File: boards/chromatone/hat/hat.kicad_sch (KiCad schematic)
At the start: 55 parts, among them J1 Pi 40-pin, J2 Strip, J3 Line out, U1 ISO7720D, U2 PCM5102A, U3 ME6211C33, U4 24LC32

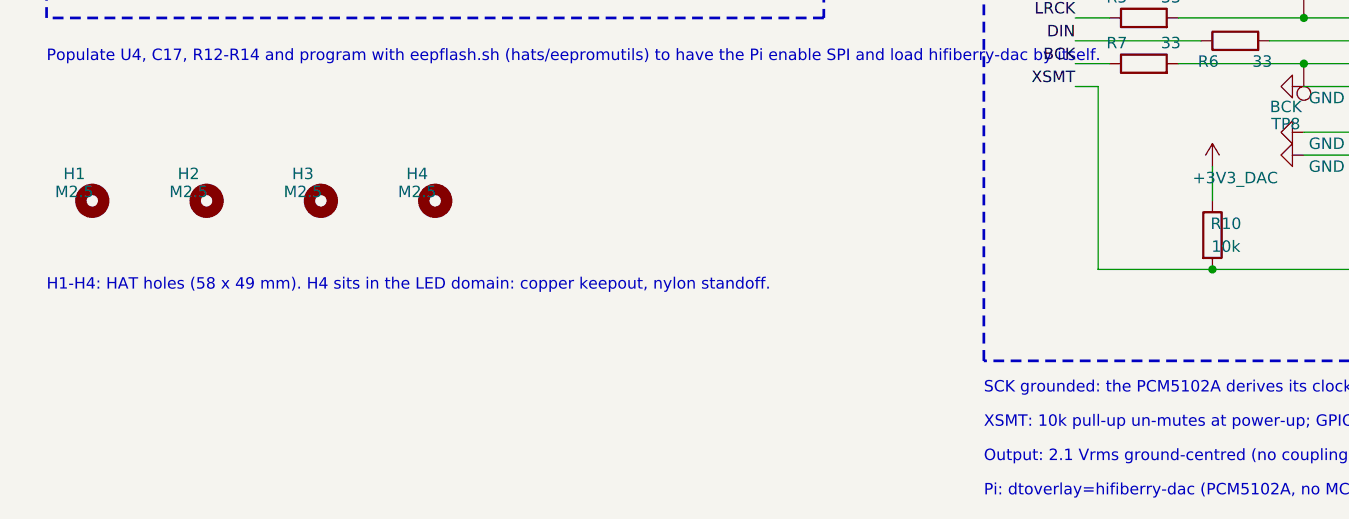
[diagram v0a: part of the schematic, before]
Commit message: chromatone/hat: Codex review round 1 fixes (holes/test points out of the CPL, H3 note, ordering notes)
Co-Authored-By: Claude Fable 5.1 <noreply@anthropic.com>
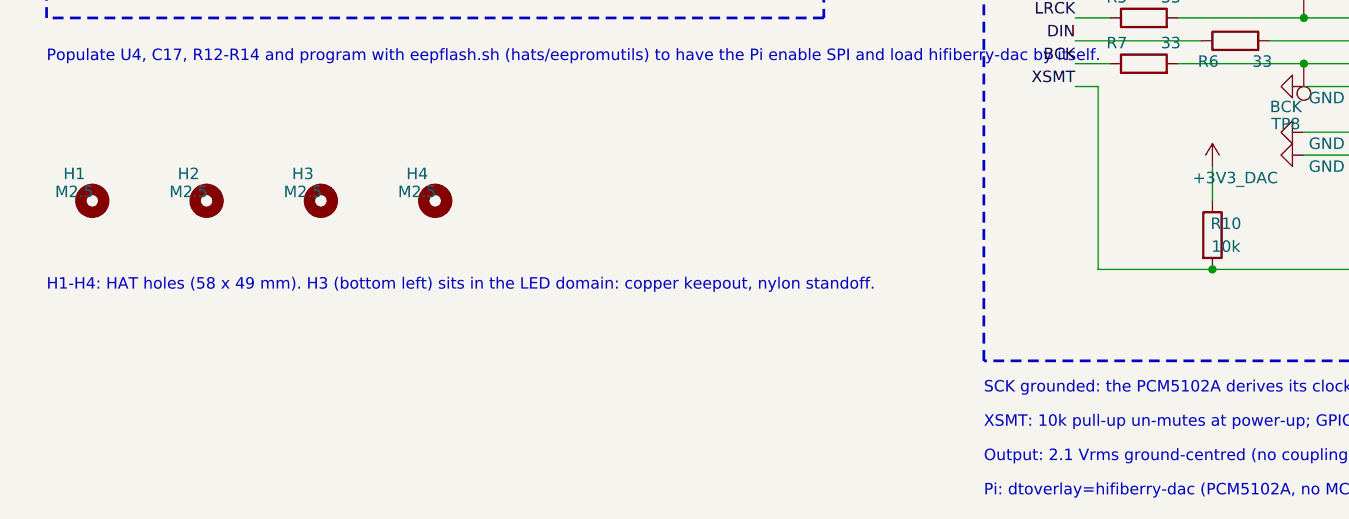
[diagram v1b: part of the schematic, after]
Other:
- note added: "H1-H4: HAT holes (58 x 49 mm). H3 (bottom left) sits in the LED domain: copper keepout, nylon standoff."
- note removed: "H1-H4: HAT holes (58 x 49 mm). H4 sits in the LED domain: copper keepout, nylon standoff."
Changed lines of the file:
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@@
 		(in_bom no)
 		(on_board yes)
+		(in_pos_files no)
 		(dnp no)
 		(property "Reference" "TP1"
@@
 		(in_bom no)
 		(on_board yes)
+		(in_pos_files no)
 		(dnp no)
 		(property "Reference" "TP2"
@@
 		(in_bom no)
 		(on_board yes)
+		(in_pos_files no)
 		(dnp no)
 		(property "Reference" "TP3"
@@
 		(in_bom no)
 		(on_board yes)
+		(in_pos_files no)
 		(dnp no)
 		(property "Reference" "TP4"
@@
 		(in_bom no)
 		(on_board yes)
+		(in_pos_files no)
 		(dnp no)
 		(property "Reference" "TP5"
@@
 		(in_bom no)
 		(on_board yes)
+		(in_pos_files no)
 		(dnp no)
 		(property "Reference" "TP6"
@@
 		(in_bom no)
 		(on_board yes)
+		(in_pos_files no)
 		(dnp no)
 		(property "Reference" "TP7"
@@
 		(in_bom no)
 		(on_board yes)
+		(in_pos_files no)
 		(dnp no)
 		(property "Reference" "TP8"
@@
 		(in_bom no)
 		(on_board yes)
+		(in_pos_files no)
 		(dnp no)
 		(property "Reference" "TP9"
@@
 		(in_bom no)
 		(on_board yes)
+		(in_pos_files no)
 		(dnp no)
 		(property "Reference" "H1"
@@
 		(in_bom no)
 		(on_board yes)
+		(in_pos_files no)
 		(dnp no)
 		(property "Reference" "H2"
@@
 		(in_bom no)
 		(on_board yes)
+		(in_pos_files no)
 		(dnp no)
 		(property "Reference" "H3"
@@
 		(in_bom no)
 		(on_board yes)
+		(in_pos_files no)
 		(dnp no)
 		(property "Reference" "H4"
@@
 		)
 	)
-	(text "H1-H4: HAT holes (58 x 49 mm). H4 sits in the LED domain: copper keepout, nylon standoff."
+	(text "H1-H4: HAT holes (58 x 49 mm). H3 (bottom left) sits in the LED domain: copper keepout, nylon standoff."
 		(exclude_from_sim no)
 		(at 5.08 190.5 0)
